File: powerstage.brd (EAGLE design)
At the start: 42 x 43.5 mm, 42 parts, among them CON1 PINHEAD_1X10-2-FEMALE, CON2 BATTERY_CON-2P-XT30-RA, CON3 PINHEAD_1X10-2-FEMALE, IC5 MCP9700, Q1 BUK9K6R2-40E,115, Q2 BUK9K6R2-40E,115, Q3 BUK9K6R2-40E,115

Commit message: inner layers update
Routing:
- net PHASE_A_CURRENT_SHUNT_N: track 36.9 -> 36.3 mm
- net PHASE_B_CURRENT_SHUNT_P: track 18.0 -> 17.4 mm
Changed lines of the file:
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@@
 <layer number="14" name="Route14" color="22" fill="1" visible="no" active="no"/>
 <layer number="15" name="Route15" color="46" fill="6" visible="no" active="yes"/>
-<layer number="16" name="Bottom" color="1" fill="1" visible="yes" active="yes"/>
+<layer number="16" name="Bottom" color="1" fill="1" visible="no" active="yes"/>
 <layer number="17" name="Pads" color="2" fill="1" visible="yes" active="yes"/>
 <layer number="18" name="Vias" color="2" fill="1" visible="yes" active="yes"/>
@@
 <layer number="20" name="Dimension" color="24" fill="1" visible="yes" active="yes"/>
 <layer number="21" name="tPlace" color="7" fill="1" visible="no" active="yes"/>
-<layer number="22" name="bPlace" color="7" fill="1" visible="yes" active="yes"/>
+<layer number="22" name="bPlace" color="7" fill="1" visible="no" active="yes"/>
 <layer number="23" name="tOrigins" color="15" fill="1" visible="no" active="yes"/>
-<layer number="24" name="bOrigins" color="15" fill="1" visible="yes" active="yes"/>
+<layer number="24" name="bOrigins" color="15" fill="1" visible="no" active="yes"/>
 <layer number="25" name="tNames" color="7" fill="1" visible="no" active="yes"/>
-<layer number="26" name="bNames" color="7" fill="1" visible="yes" active="yes"/>
+<layer number="26" name="bNames" color="7" fill="1" visible="no" active="yes"/>
 <layer number="27" name="tValues" color="7" fill="1" visible="no" active="yes"/>
 <layer number="28" name="bValues" color="7" fill="1" visible="no" active="yes"/>
@@
 <layer number="50" name="dxf" color="7" fill="1" visible="no" active="yes"/>
 <layer number="51" name="tDocu" color="7" fill="1" visible="no" active="yes"/>
-<layer number="52" name="bDocu" color="7" fill="1" visible="yes" active="yes"/>
+<layer number="52" name="bDocu" color="7" fill="1" visible="no" active="yes"/>
 <layer number="53" name="tGND_GNDA" color="7" fill="9" visible="no" active="no"/>
 <layer number="54" name="bGND_GNDA" color="1" fill="9" visible="no" active="no"/>
@@
 </layers>
 <board>
-<fusionsync huburn="a.cGVyc29uYWw6dWUyYWE4ZDY4" projecturn="a.cGVyc29uYWw6dWUyYWE4ZDY4IzIwMTgxMTA4MTU5MTUwNTA2" f3durn="urn:adsk.wipprod:dm.lineage:PNkJALQsRiGXmceaXmEg1A" pcbguid="a30d68d2-795d-4aa0-9250-ee42eeb516a6" lastpulledtime="" lastsyncedchangeguid="d8c6bf63-8608-d522-5299-755ff265eaea"/>
+<fusionsync huburn="a.cGVyc29uYWw6dWUyYWE4ZDY4" projecturn="a.cGVyc29uYWw6dWUyYWE4ZDY4IzIwMTgxMTA4MTU5MTUwNTA2" f3durn="urn:adsk.wipprod:dm.lineage:PNkJALQsRiGXmceaXmEg1A" pcbguid="a30d68d2-795d-4aa0-9250-ee42eeb516a6" lastpulledtime="" lastsyncedchangeguid="5c4f4f1c-28fc-b0fa-ed4d-baeeaa0fb5fd"/>
 <plain>
 <wire x1="0" y1="0" x2="0" y2="21" width="0.1524" layer="49" style="shortdash" locked="yes"/>
@@
 </autorouter>
 <elements>
-<element name="A" library="PADS" library_urn="urn:adsk.eagle:library:3188696" package="HOLE_2" package3d_urn="urn:adsk.eagle:package:4854323/1" value="PAD-HOLE_2" x="5" y="18" smashed="yes">
+<element name="A" library="PADS" library_urn="urn:adsk.eagle:library:3188696" package="HOLE_2" package3d_urn="urn:adsk.eagle:package:4854323/1" value="PAD-HOLE_2" x="5" y="18" locked="yes" smashed="yes">
 <attribute name="BOM" value="EXCLUDE" x="5" y="18" size="1.778" layer="27" display="off"/>
 <attribute name="NAME" x="5" y="20" size="1" layer="25" font="vector" ratio="15" align="center"/>
@@
 <attribute name="VALUE" x="14.7" y="1.75" size="0.5" layer="27" font="vector" ratio="15" rot="R180" align="center"/>
 </element>
-<element name="B" library="PADS" library_urn="urn:adsk.eagle:library:3188696" package="HOLE_2" package3d_urn="urn:adsk.eagle:package:4854323/1" value="PAD-HOLE_2" x="-5" y="18" smashed="yes">
+<element name="B" library="PADS" library_urn="urn:adsk.eagle:library:3188696" package="HOLE_2" package3d_urn="urn:adsk.eagle:package:4854323/1" value="PAD-HOLE_2" x="-5" y="18" locked="yes" smashed="yes">
 <attribute name="BOM" value="EXCLUDE" x="-5" y="18" size="1.778" layer="27" display="off"/>
 <attribute name="NAME" x="-5" y="20" size="1" layer="25" font="vector" ratio="15" align="center"/>
@@
 <attribute name="VALUE" x="-14.7" y="-2.05" size="0.5" layer="27" font="vector" ratio="15" align="center"/>
 </element>
-<element name="C" library="PADS" library_urn="urn:adsk.eagle:library:3188696" package="HOLE_2" package3d_urn="urn:adsk.eagle:package:4854323/1" value="PAD-HOLE_2" x="0" y="18" smashed="yes">
+<element name="C" library="PADS" library_urn="urn:adsk.eagle:library:3188696" package="HOLE_2" package3d_urn="urn:adsk.eagle:package:4854323/1" value="PAD-HOLE_2" x="0" y="18" locked="yes" smashed="yes">
 <attribute name="BOM" value="EXCLUDE" x="0" y="18" size="1.778" layer="27" display="off"/>
 <attribute name="NAME" x="0" y="20" size="1" layer="25" font="vector" ratio="15" align="center"/>
@@
 <vertex x="11.125" y="8.825"/>
 </polygon>
-<polygon width="0.3" layer="2">
+<polygon width="0.2" layer="2">
 <vertex x="-17.2" y="19.4"/>
 <vertex x="-17.2" y="-20"/>
@@
 <contactref element="Q2" pad="1"/>
 <wire x1="4.595" y1="8.8" x2="4.595" y2="9.2" width="0.1524" layer="1"/>
-<polygon width="0.1524" layer="1" thermals="no">
+<polygon width="0.2" layer="1" thermals="no">
 <vertex x="6.7" y="9.8"/>
 <vertex x="6.7" y="15.7"/>
@@
 <wire x1="7.2128625" y1="1.65" x2="8.4" y2="2.8371375" width="0.15" layer="15"/>
 <contactref element="CON1" pad="8"/>
-<wire x1="-16.6" y1="4.05" x2="-17.5" y2="4.95" width="0.15" layer="15"/>
-<wire x1="-17.5" y1="4.95" x2="-17.2" y2="5" width="0.15" layer="15"/>
+<wire x1="-16.25" y1="4.05" x2="-17.2" y2="5" width="0.15" layer="15"/>
 <wire x1="7.2128625" y1="1.65" x2="-12.7378625" y2="1.65" width="0.15" layer="15"/>
 <wire x1="-12.7378625" y1="1.65" x2="-15.1378625" y2="4.05" width="0.15" layer="15"/>
-<wire x1="-15.1378625" y1="4.05" x2="-16.6" y2="4.05" width="0.15" layer="15"/>
+<wire x1="-15.1378625" y1="4.05" x2="-16.25" y2="4.05" width="0.15" layer="15"/>
 </signal>
 <signal name="PHASE_A_CURRENT_SHUNT_P">
@@
 <wire x1="-15.30606875" y1="3.74393125" x2="-12.9121375" y2="1.35" width="0.15" layer="15"/>
 <contactref element="CON1" pad="7"/>
-<wire x1="-15.30606875" y1="3.74393125" x2="-16.60606875" y2="3.74393125" width="0.15" layer="15"/>
-<wire x1="-16.60606875" y1="3.74393125" x2="-17.35" y2="3" width="0.15" layer="15"/>
-<wire x1="-17.2" y1="3" x2="-17.35" y2="3" width="0.15" layer="15"/>
+<wire x1="-15.30606875" y1="3.74393125" x2="-16.28106875" y2="3.74393125" width="0.15" layer="15"/>
+<wire x1="-16.28106875" y1="3.74393125" x2="-17.025" y2="3" width="0.15" layer="15"/>
+<wire x1="-17.025" y1="3" x2="-17.2" y2="3" width="0.15" layer="15"/>
 <wire x1="-12.9121375" y1="1.35" x2="7.3871375" y2="1.35" width="0.15" layer="15"/>
 </signal>
@@
 <wire x1="-10.7378625" y1="6.65" x2="-12.2878625" y2="8.2" width="0.15" layer="15"/>
 <wire x1="-10.7378625" y1="6.65" x2="-8.4378625" y2="6.65" width="0.15" layer="15"/>
-<wire x1="-16.7" y1="8.2" x2="-17.2" y2="9" width="0.15" layer="15"/>
-<wire x1="-12.2878625" y1="8.2" x2="-16.7" y2="8.2" width="0.15" layer="15"/>
+<wire x1="-16.4" y1="8.2" x2="-17.2" y2="9" width="0.15" layer="15"/>
+<wire x1="-12.2878625" y1="8.2" x2="-16.4" y2="8.2" width="0.15" layer="15"/>
 </signal>
 <signal name="PHASE_B_CURRENT_SHUNT_P">
@@
 <wire x1="-8.15" y1="5.55" x2="-8.15" y2="5.9378625" width="0.15" layer="15"/>
 <wire x1="-8.5621375" y1="6.35" x2="-8.15" y2="5.9378625" width="0.15" layer="15"/>
-<wire x1="-16.7" y1="7.9" x2="-17.5" y2="7.1" width="0.15" layer="15"/>
-<wire x1="-17.5" y1="7.1" x2="-17.2" y2="7" width="0.15" layer="15"/>
-<wire x1="-16.7" y1="7.9" x2="-12.4121375" y2="7.9" width="0.15" layer="15"/>
+<wire x1="-16.4" y1="7.9" x2="-17.2" y2="7.1" width="0.15" layer="15"/>
+<wire x1="-17.2" y1="7.1" x2="-17.2" y2="7" width="0.15" layer="15"/>
+<wire x1="-16.4" y1="7.9" x2="-12.4121375" y2="7.9" width="0.15" layer="15"/>
 <wire x1="-12.4121375" y1="7.9" x2="-10.8621375" y2="6.35" width="0.15" layer="15"/>
 <wire x1="-10.8621375" y1="6.35" x2="-8.5621375" y2="6.35" width="0.15" layer="15"/>
@@
 <contactref element="Q3" pad="5" route="any" routetag="T2.D"/>
 <contactref element="Q3" pad="1"/>
-<polygon width="0.1524" layer="1" thermals="no" rank="3">
+<polygon width="0.2" layer="1" thermals="no" rank="3">
 <vertex x="0.2" y="9.8"/>
 <vertex x="0.2" y="15.8"/>
@@
 <contactref element="Q1" pad="1"/>
 <contactref element="B" pad="P$1"/>
-<polygon width="0.1524" layer="1" thermals="no" rank="2">
+<polygon width="0.2" layer="1" thermals="no" rank="2">
 <vertex x="-6.45" y="9.8"/>
 <vertex x="-6.45" y="19.4"/>
@@
 <vertex x="-2.9" y="9.8"/>
 </polygon>
-<wire x1="-8.405" y1="8.8" x2="-8.405" y2="3.295" width="0.25" layer="1"/>
-<wire x1="-8.405" y1="3.295" x2="-11.8" y2="-0.1" width="0.25" layer="1"/>
+<wire x1="-8.405" y1="8.8" x2="-8.33" y2="8.725" width="0.25" layer="1"/>
+<wire x1="-8.33" y1="8.725" x2="-8.33" y2="3.37" width="0.25" layer="1"/>
+<wire x1="-8.33" y1="3.37" x2="-11.8" y2="-0.1" width="0.25" layer="1"/>
 <polygon width="0.1524" layer="1" thermals="no">
 <vertex x="-8.15" y="9.35"/>

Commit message: poly update
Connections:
- net PGND: now also CON2.P$3, CON2.P$4
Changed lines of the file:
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@@
 <drawing>
 <settings>
-<setting alwaysvectorfont="yes"/>
+<setting alwaysvectorfont="no"/>
 <setting verticaltext="up"/>
 </settings>
-<grid distance="0.025" unitdist="mm" unit="mm" style="lines" multiple="1" display="no" altdistance="5" altunitdist="mil" altunit="mil"/>
+<grid distance="0.25" unitdist="mm" unit="mm" style="lines" multiple="1" display="yes" altdistance="5" altunitdist="mil" altunit="mil"/>
 <layers>
 <layer number="1" name="Top" color="4" fill="1" visible="no" active="yes"/>
-<layer number="2" name="Route2" color="43" fill="3" visible="yes" active="yes"/>
+<layer number="2" name="Route2" color="43" fill="3" visible="no" active="yes"/>
 <layer number="3" name="Route3" color="17" fill="1" visible="no" active="no"/>
 <layer number="4" name="Route4" color="18" fill="1" visible="no" active="no"/>
@@
 <layer number="14" name="Route14" color="22" fill="1" visible="no" active="no"/>
 <layer number="15" name="Route15" color="46" fill="6" visible="no" active="yes"/>
-<layer number="16" name="Bottom" color="1" fill="1" visible="no" active="yes"/>
+<layer number="16" name="Bottom" color="1" fill="1" visible="yes" active="yes"/>
 <layer number="17" name="Pads" color="2" fill="1" visible="yes" active="yes"/>
 <layer number="18" name="Vias" color="2" fill="1" visible="yes" active="yes"/>
@@
 <layer number="20" name="Dimension" color="24" fill="1" visible="yes" active="yes"/>
 <layer number="21" name="tPlace" color="7" fill="1" visible="no" active="yes"/>
-<layer number="22" name="bPlace" color="7" fill="1" visible="no" active="yes"/>
+<layer number="22" name="bPlace" color="7" fill="1" visible="yes" active="yes"/>
 <layer number="23" name="tOrigins" color="15" fill="1" visible="no" active="yes"/>
-<layer number="24" name="bOrigins" color="15" fill="1" visible="no" active="yes"/>
+<layer number="24" name="bOrigins" color="15" fill="1" visible="yes" active="yes"/>
 <layer number="25" name="tNames" color="7" fill="1" visible="no" active="yes"/>
-<layer number="26" name="bNames" color="7" fill="1" visible="no" active="yes"/>
-<layer number="27" name="tValues" color="7" fill="1" visible="no" active="yes"/>
+<layer number="26" name="bNames" color="7" fill="1" visible="yes" active="yes"/>
+<layer number="27" name="tValues" color="7" fill="1" visible="yes" active="yes"/>
 <layer number="28" name="bValues" color="7" fill="1" visible="no" active="yes"/>
 <layer number="29" name="tStop" color="7" fill="3" visible="no" active="yes"/>
@@
 <layer number="50" name="dxf" color="7" fill="1" visible="no" active="yes"/>
 <layer number="51" name="tDocu" color="7" fill="1" visible="no" active="yes"/>
-<layer number="52" name="bDocu" color="7" fill="1" visible="no" active="yes"/>
+<layer number="52" name="bDocu" color="7" fill="1" visible="yes" active="yes"/>
 <layer number="53" name="tGND_GNDA" color="7" fill="9" visible="no" active="no"/>
 <layer number="54" name="bGND_GNDA" color="1" fill="9" visible="no" active="no"/>
@@
 <contactref element="CON2" pad="-"/>
 <polygon width="0.1524" layer="16" rank="5">
-<vertex x="0" y="19.4"/>
+<vertex x="17.2" y="19.4"/>
 <vertex x="-17.2" y="19.4"/>
 <vertex x="-17.2" y="-20"/>
+<vertex x="-6.75" y="-20"/>
+<vertex x="-6.75" y="-22"/>
+<vertex x="-4.5" y="-22"/>
+<vertex x="-4.5" y="-20"/>
+<vertex x="4.5" y="-20"/>
+<vertex x="4.5" y="-22"/>
+<vertex x="6.75" y="-22"/>
+<vertex x="6.75" y="-20"/>
 <vertex x="17.2" y="-20"/>
-<vertex x="17.2" y="19.4"/>
 </polygon>
 <via x="13.3" y="6.8" extent="1-16" drill="0.3" diameter="0.6"/>
@@
 <contactref element="D3" pad="A"/>
 <contactref element="D4" pad="A"/>
+<contactref element="CON2" pad="P$3"/>
+<contactref element="CON2" pad="P$4"/>
 </signal>
 <signal name="N$3">

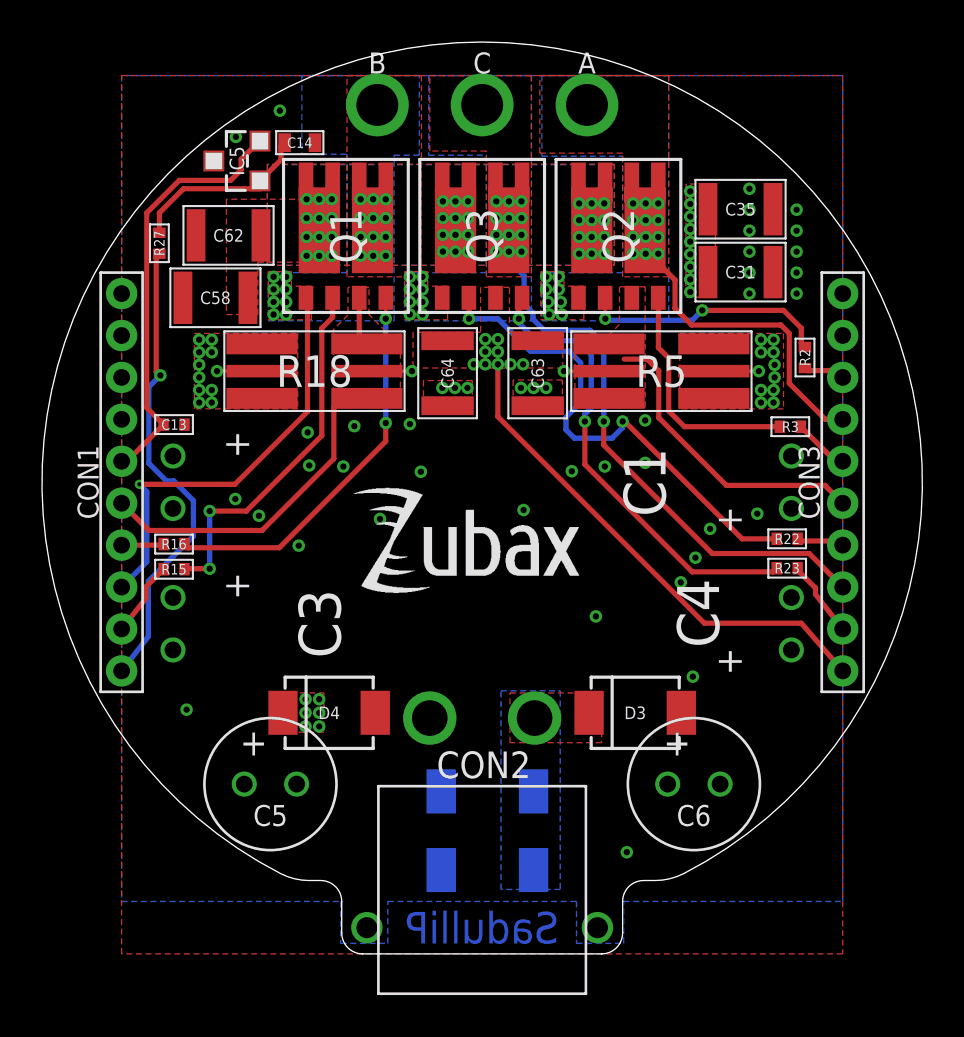
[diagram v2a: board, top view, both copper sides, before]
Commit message: pinout fixes
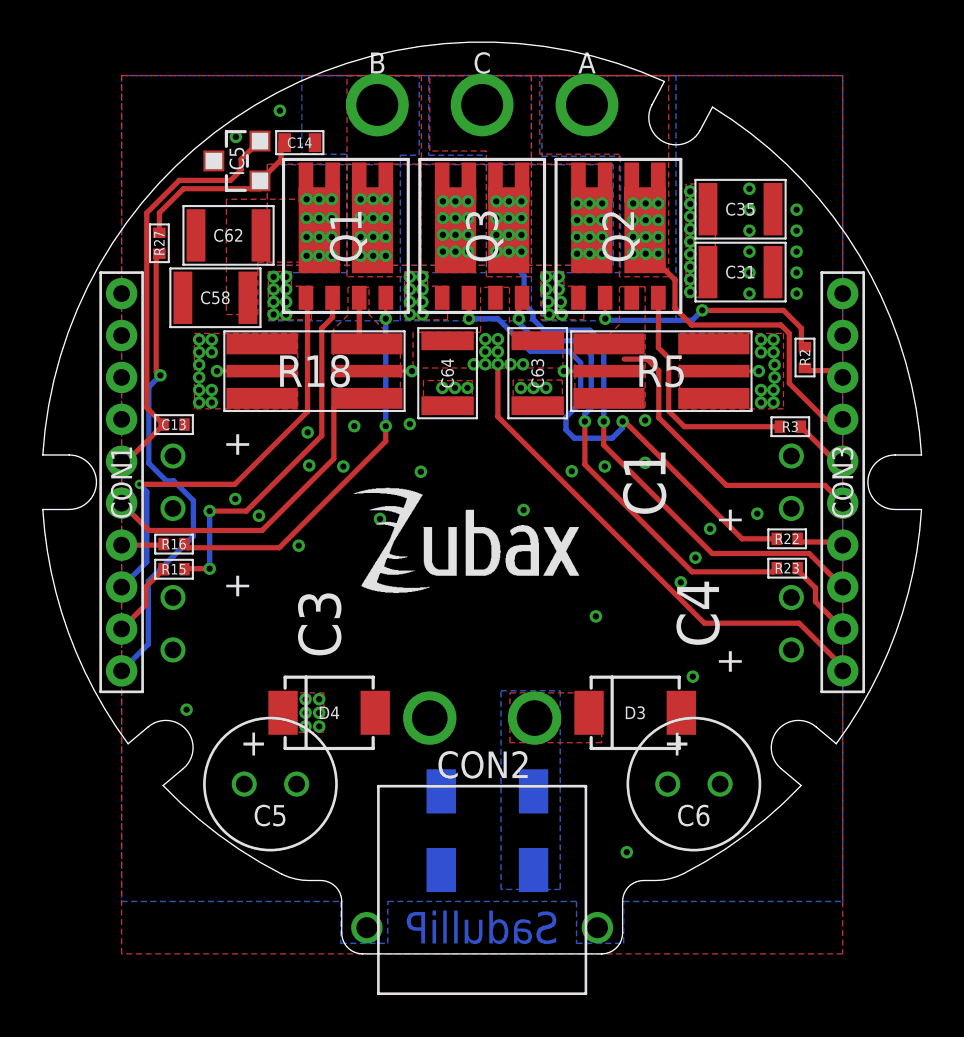
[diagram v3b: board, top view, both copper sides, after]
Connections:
- removed net GND: CON3.10
- net PGND: now also CON3.10
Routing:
- net VDC: track 0.80 -> 0.22 mm
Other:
- board size 42 x 43.5 mm -> 41.9 x 43.5 mm
